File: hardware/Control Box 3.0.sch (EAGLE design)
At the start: 27 parts, among them IC1 LM324N, J1 AC_IN, J2 To_Relay, J3 From_Relay, J4 AC_OUT, J5 To_Reg, J6 From_Reg, J7 54601-908WPLFW/MODEL, K1 T9AS1D22-54PIN, K2 T9AS1D22-54PIN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

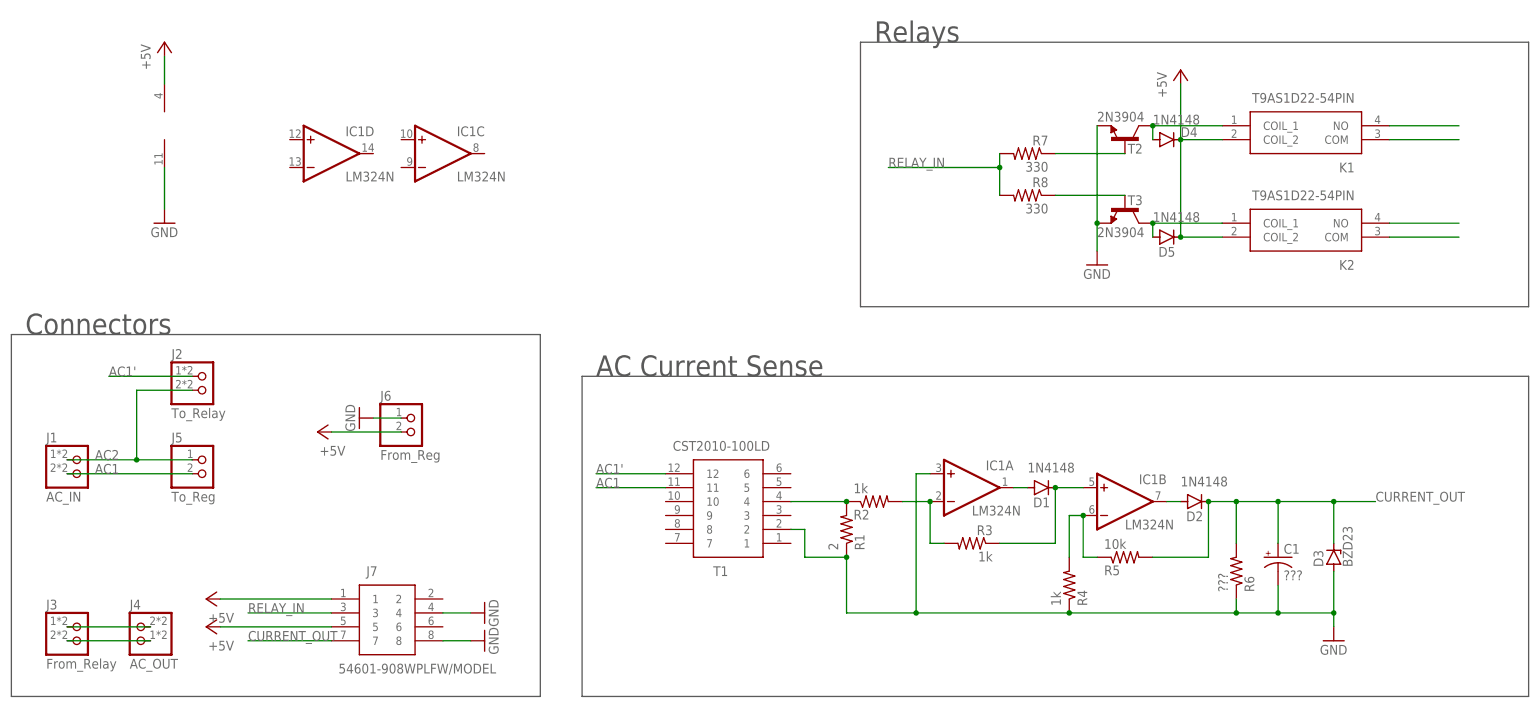
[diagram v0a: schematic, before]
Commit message: Replace LM324 with LM358, clean up component names, silkscreen layout, and some routing
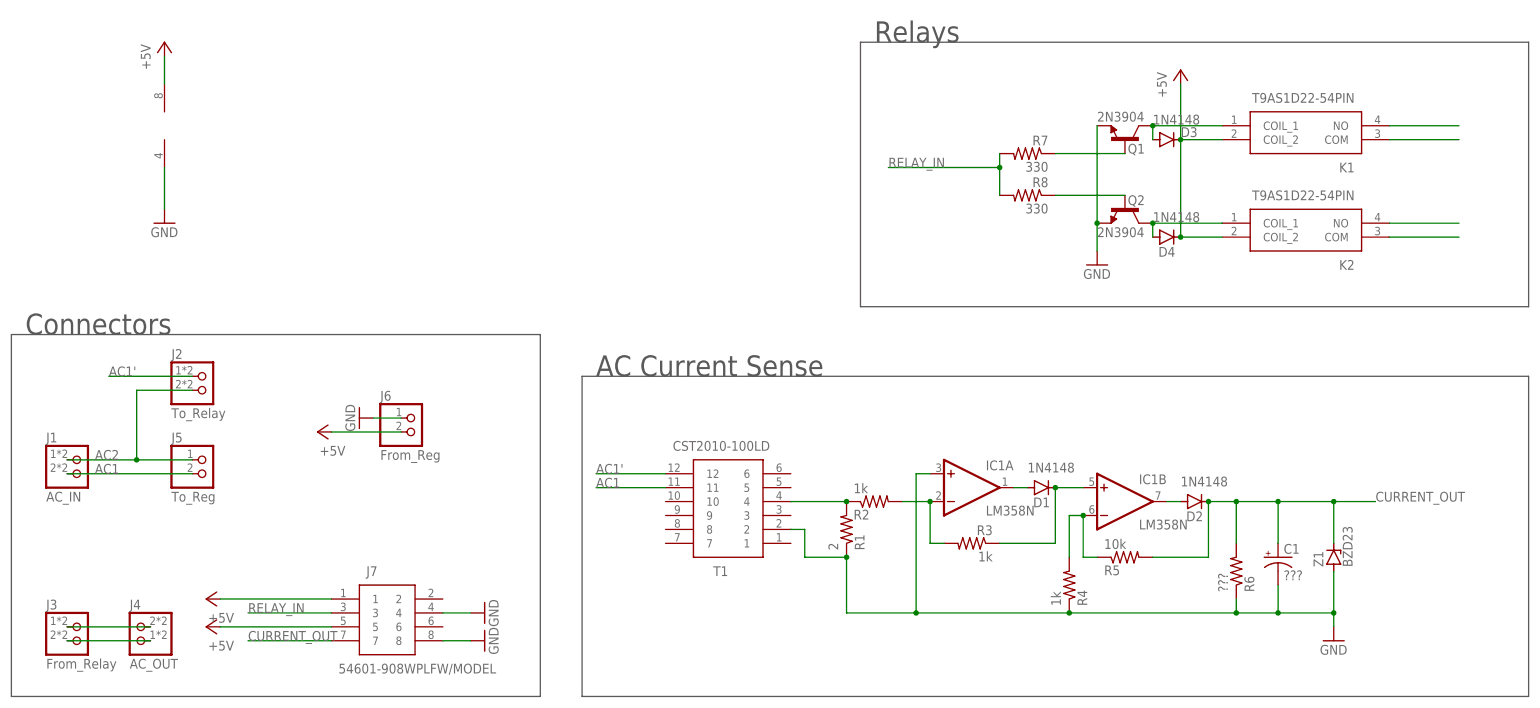
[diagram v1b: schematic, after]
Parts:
- removed D5: 1N4148, diode:1N4148DO35-7
- added Z1: BZD23, diode:BZD23
- D3: value BZD23 -> 1N4148; device diode:BZD23 -> diode:1N4148DO35-7
- IC1: value LM324N -> LM358N; device mcp:LM324N -> linear:LM358N
- renumbered T2 to Q1, T3 to Q2
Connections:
- net +5V: now also D3.C; no longer D5.C
- net CURRENT_OUT: now also Z1.C; no longer D3.C
- net GND: now also Z1.A; no longer D3.A
- net N$11: now also D4.A; no longer D5.A
- net N$8: now also D3.A; no longer D4.A
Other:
- moved on the sheet: D4

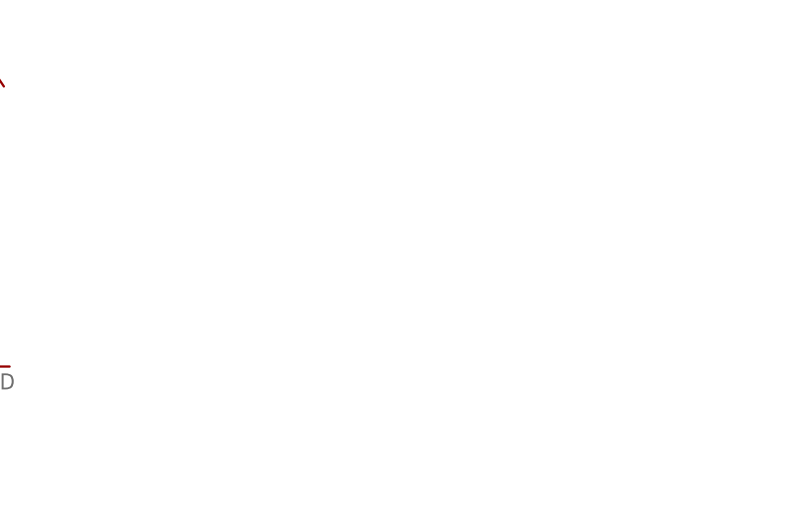
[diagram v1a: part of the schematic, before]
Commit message: add power indication led to relay module
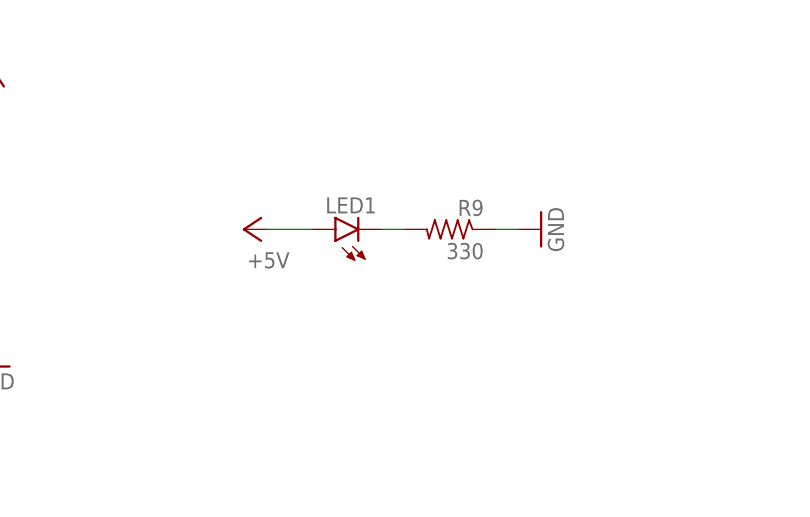
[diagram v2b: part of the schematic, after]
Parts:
- added LED1: (no value), led:LED5MM
- added R9: 330, mcp:R-US
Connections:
- new net N$17: LED1.C, R9.2
- net +5V: now also LED1.A
- net GND: now also R9.1
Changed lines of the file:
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@@
 <part name="D4" library="diode" library_urn="urn:adsk.eagle:library:210" deviceset="1N4148" device="DO35-7" package3d_urn="urn:adsk.eagle:package:43339/2" value="1N4148"/>
 <part name="IC1" library="linear" library_urn="urn:adsk.eagle:library:262" deviceset="LM358" device="N" package3d_urn="urn:adsk.eagle:package:16409/2"/>
+<part name="LED1" library="led" library_urn="urn:adsk.eagle:library:259" deviceset="LED" device="5MM" package3d_urn="urn:adsk.eagle:package:15799/2"/>
+<part name="R9" library="mcp" library_urn="urn:adsk.eagle:library:9418757" deviceset="R-US" device="" package3d_urn="urn:adsk.eagle:package:23498/2" value="330"/>
+<part name="+5V6" library="supply1" library_urn="urn:adsk.eagle:library:371" deviceset="+5V" device=""/>
+<part name="GND7" library="supply1" library_urn="urn:adsk.eagle:library:371" deviceset="GND" device=""/>
 </parts>
 <sheets>
@@
 </instance>
 <instance part="IC1" gate="P" x="30.48" y="109.22" smashed="yes"/>
+<instance part="LED1" gate="G$1" x="68.58" y="106.68" smashed="yes" rot="R90">
+<attribute name="NAME" x="73.152" y="110.236" size="1.778" layer="95" rot="R180"/>
+<attribute name="VALUE" x="73.152" y="112.395" size="1.778" layer="96" rot="R180"/>
+</instance>
+<instance part="R9" gate="G$1" x="81.28" y="106.68" smashed="yes" rot="MR0">
+<attribute name="NAME" x="85.09" y="108.1786" size="1.778" layer="95" rot="MR0"/>
+<attribute name="VALUE" x="85.09" y="103.378" size="1.778" layer="96" rot="MR0"/>
+</instance>
+<instance part="+5V6" gate="1" x="58.42" y="106.68" smashed="yes" rot="R90">
+<attribute name="VALUE" x="63.5" y="104.14" size="1.778" layer="96" rot="R180"/>
+</instance>
+<instance part="GND7" gate="1" x="91.44" y="106.68" smashed="yes" rot="R90">
+<attribute name="VALUE" x="93.98" y="104.14" size="1.778" layer="96" rot="R90"/>
+</instance>
 </instances>
 <busses>
@@
 <junction x="200.66" y="91.44"/>
 </segment>
+<segment>
+<pinref part="R9" gate="G$1" pin="1"/>
+<pinref part="GND7" gate="1" pin="GND"/>
+<wire x1="86.36" y1="106.68" x2="88.9" y2="106.68" width="0.1524" layer="91"/>
+</segment>
 </net>
 <net name="N$2" class="0">
@@
 <pinref part="D4" gate="G$1" pin="C"/>
 <junction x="215.9" y="88.9"/>
+</segment>
+<segment>
+<pinref part="+5V6" gate="1" pin="+5V"/>
+<pinref part="LED1" gate="G$1" pin="A"/>
+<wire x1="60.96" y1="106.68" x2="66.04" y2="106.68" width="0.1524" layer="91"/>
 </segment>
 </net>
@@
 </segment>
 </net>
+<net name="N$17" class="0">
+<segment>
+<pinref part="LED1" gate="G$1" pin="C"/>
+<pinref part="R9" gate="G$1" pin="2"/>
+<wire x1="73.66" y1="106.68" x2="76.2" y2="106.68" width="0.1524" layer="91"/>
+</segment>
+</net>

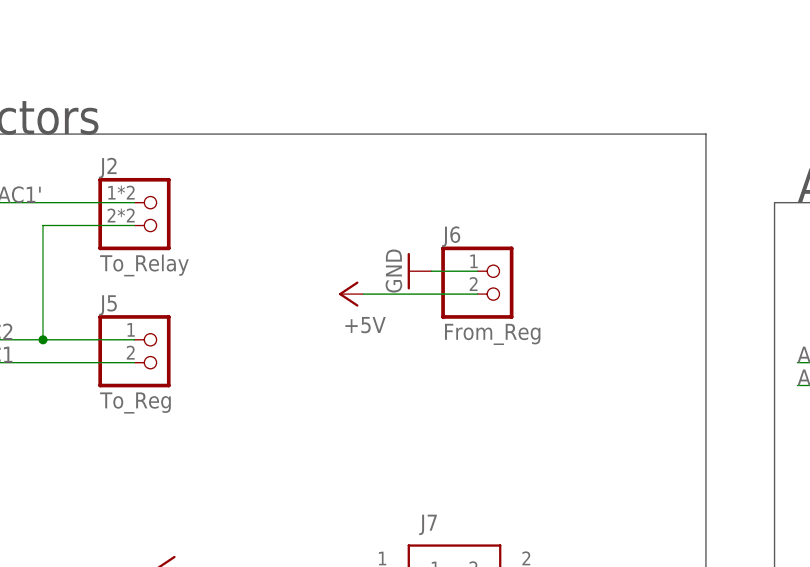
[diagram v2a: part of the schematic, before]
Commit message: fix VH connectors on relay module
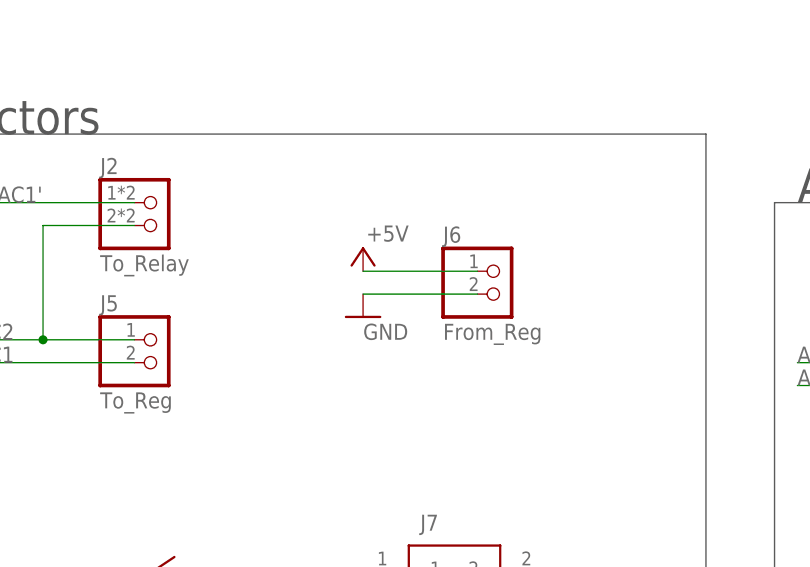
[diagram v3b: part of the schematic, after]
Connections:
- net +5V: now also J6.1; no longer J6.2
- net GND: now also J6.2; no longer J6.1
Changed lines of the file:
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@@
 <parts>
 <part name="J7" library="mcp" library_urn="urn:adsk.eagle:library:9418757" deviceset="54601-908WPLF" device="W/MODEL" package3d_urn="urn:adsk.eagle:package:9475071/4"/>
-<part name="T1" library="mcp" library_urn="urn:adsk.eagle:library:9418757" deviceset="CST2010-100LD" device=""/>
+<part name="T1" library="mcp" library_urn="urn:adsk.eagle:library:9418757" deviceset="CST2010-100LD" device="" package3d_urn="urn:adsk.eagle:package:10310781/1"/>
 <part name="R1" library="mcp" library_urn="urn:adsk.eagle:library:9418757" deviceset="R-US" device="" package3d_urn="urn:adsk.eagle:package:23498/2" value="2"/>
 <part name="D1" library="diode" library_urn="urn:adsk.eagle:library:210" deviceset="1N4148" device="DO35-7" package3d_urn="urn:adsk.eagle:package:43339/2" value="1N4148"/>
@@
 <part name="C1" library="rcl" library_urn="urn:adsk.eagle:library:334" deviceset="CPOL-US" device="E1.8-4" package3d_urn="urn:adsk.eagle:package:23336/2" value="???"/>
 <part name="D2" library="diode" library_urn="urn:adsk.eagle:library:210" deviceset="1N4148" device="DO35-7" package3d_urn="urn:adsk.eagle:package:43339/2" value="1N4148"/>
-<part name="J1" library="mcp" library_urn="urn:adsk.eagle:library:9418757" deviceset="VC0200500000G" device="VC0200500000G" package3d_urn="urn:adsk.eagle:package:10227406/1" value="AC_IN"/>
-<part name="J5" library="mcp" library_urn="urn:adsk.eagle:library:9418757" deviceset="VH_1X2" device="GAP" package3d_urn="urn:adsk.eagle:package:10227928/1" value="To_Reg"/>
-<part name="J6" library="mcp" library_urn="urn:adsk.eagle:library:9418757" deviceset="VH_1X2" device="" package3d_urn="urn:adsk.eagle:package:10227910/1" value="From_Reg"/>
-<part name="J3" library="mcp" library_urn="urn:adsk.eagle:library:9418757" deviceset="VC0200500000G" device="VC0200500000G" package3d_urn="urn:adsk.eagle:package:10227406/1" value="From_Relay"/>
+<part name="J1" library="mcp" library_urn="urn:adsk.eagle:library:9418757" deviceset="VC0200500000G" device="VC0200500000G" package3d_urn="urn:adsk.eagle:package:10227406/2" value="AC_IN"/>
+<part name="J5" library="mcp" library_urn="urn:adsk.eagle:library:9418757" deviceset="VH_1X2" device="GAP" package3d_urn="urn:adsk.eagle:package:10227928/3" value="To_Reg"/>
+<part name="J6" library="mcp" library_urn="urn:adsk.eagle:library:9418757" deviceset="VH_1X2" device="" package3d_urn="urn:adsk.eagle:package:10227910/4" value="From_Reg"/>
+<part name="J3" library="mcp" library_urn="urn:adsk.eagle:library:9418757" deviceset="VC0200500000G" device="VC0200500000G" package3d_urn="urn:adsk.eagle:package:10227406/2" value="From_Relay"/>
 <part name="+5V1" library="supply1" library_urn="urn:adsk.eagle:library:371" deviceset="+5V" device=""/>
 <part name="GND1" library="supply1" library_urn="urn:adsk.eagle:library:371" deviceset="GND" device=""/>
@@
 <part name="+5V3" library="supply1" library_urn="urn:adsk.eagle:library:371" deviceset="+5V" device=""/>
 <part name="+5V4" library="supply1" library_urn="urn:adsk.eagle:library:371" deviceset="+5V" device=""/>
-<part name="K1" library="mcp" library_urn="urn:adsk.eagle:library:9418757" deviceset="T9AS1D22-5" device="4PIN"/>
-<part name="K2" library="mcp" library_urn="urn:adsk.eagle:library:9418757" deviceset="T9AS1D22-5" device="4PIN"/>
-<part name="J2" library="mcp" library_urn="urn:adsk.eagle:library:9418757" deviceset="VC0200500000G" device="VC0200500000G" package3d_urn="urn:adsk.eagle:package:10227406/1" value="To_Relay"/>
-<part name="J4" library="mcp" library_urn="urn:adsk.eagle:library:9418757" deviceset="VC0200500000G" device="VC0200500000G" package3d_urn="urn:adsk.eagle:package:10227406/1" value="AC_OUT"/>
+<part name="K1" library="mcp" library_urn="urn:adsk.eagle:library:9418757" deviceset="T9AS1D22-5" device="4PIN" package3d_urn="urn:adsk.eagle:package:10310780/1"/>
+<part name="K2" library="mcp" library_urn="urn:adsk.eagle:library:9418757" deviceset="T9AS1D22-5" device="4PIN" package3d_urn="urn:adsk.eagle:package:10310780/1"/>
+<part name="J2" library="mcp" library_urn="urn:adsk.eagle:library:9418757" deviceset="VC0200500000G" device="VC0200500000G" package3d_urn="urn:adsk.eagle:package:10227406/2" value="To_Relay"/>
+<part name="J4" library="mcp" library_urn="urn:adsk.eagle:library:9418757" deviceset="VC0200500000G" device="VC0200500000G" package3d_urn="urn:adsk.eagle:package:10227406/2" value="AC_OUT"/>
 <part name="Q1" library="transistor" library_urn="urn:adsk.eagle:library:402" deviceset="2N3904" device="" package3d_urn="urn:adsk.eagle:package:28523/2"/>
 <part name="Q2" library="transistor" library_urn="urn:adsk.eagle:library:402" deviceset="2N3904" device="" package3d_urn="urn:adsk.eagle:package:28523/2"/>
@@
 <attribute name="VALUE" x="8.89" y="10.16" size="1.778" layer="96"/>
 </instance>
-<instance part="+5V1" gate="1" x="58.42" y="53.34" smashed="yes" rot="R90">
-<attribute name="VALUE" x="63.5" y="50.8" size="1.778" layer="96" rot="R180"/>
-</instance>
-<instance part="GND1" gate="1" x="66.04" y="55.88" smashed="yes" rot="R270">
-<attribute name="VALUE" x="63.5" y="58.42" size="1.778" layer="96" rot="R270"/>
+<instance part="+5V1" gate="1" x="60.96" y="58.42" smashed="yes">
+<attribute name="VALUE" x="66.04" y="60.96" size="1.778" layer="96" rot="R180"/>
+</instance>
+<instance part="GND1" gate="1" x="60.96" y="50.8" smashed="yes">
+<attribute name="VALUE" x="60.96" y="48.26" size="1.778" layer="96"/>
 </instance>
 <instance part="GND2" gate="1" x="30.48" y="91.44" smashed="yes">
@@
 <nets>
 <net name="GND" class="2">
-<segment>
-<pinref part="GND1" gate="1" pin="GND"/>
-<pinref part="J6" gate="G$1" pin="1"/>
-<wire x1="68.58" y1="55.88" x2="73.66" y2="55.88" width="0.1524" layer="91"/>
-</segment>
 <segment>
 <wire x1="30.48" y1="101.6" x2="30.48" y2="93.98" width="0.1524" layer="91"/>
@@
 <wire x1="86.36" y1="106.68" x2="88.9" y2="106.68" width="0.1524" layer="91"/>
 </segment>
+<segment>
+<pinref part="GND1" gate="1" pin="GND"/>
+<pinref part="J6" gate="G$1" pin="2"/>
+<wire x1="60.96" y1="53.34" x2="73.66" y2="53.34" width="0.1524" layer="91"/>
+</segment>
 </net>
 <net name="N$2" class="0">
@@
 </net>
 <net name="+5V" class="2">
-<segment>
-<pinref part="+5V1" gate="1" pin="+5V"/>
-<pinref part="J6" gate="G$1" pin="2"/>
-<wire x1="60.96" y1="53.34" x2="73.66" y2="53.34" width="0.1524" layer="91"/>
-</segment>
 <segment>
 <wire x1="30.48" y1="116.84" x2="30.48" y2="121.92" width="0.1524" layer="91"/>
@@
 <wire x1="60.96" y1="106.68" x2="66.04" y2="106.68" width="0.1524" layer="91"/>
 </segment>
-</net>
+<segment>
+<pinref part="+5V1" gate="1" pin="+5V"/>
+<pinref part="J6" gate="G$1" pin="1"/>
+<wire x1="60.96" y1="55.88" x2="73.66" y2="55.88" width="0.1524" layer="91"/>
+</segment>
+</net>
